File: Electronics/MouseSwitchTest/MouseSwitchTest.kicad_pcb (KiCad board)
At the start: 2 copper layers, 20.3 x 19.1 mm, 4 parts

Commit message: updated the middle click pcb
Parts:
- moved VDD1 14.1 mm to (13.5, 6.76)
- moved GPIO1 9.00 mm to (10.9, 6.76)
- moved S1 5.10 mm to (7.05, 0.00), turned to 180 degrees
- moved NC1 3.92 mm to (8.41, 6.76)
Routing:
- net Net-(NC1-Pin): track 7.81 -> 11.1 mm
- net Net-(GPIO1-Pin): track 6.76 -> 8.37 mm
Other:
- board size 20.3 x 19.1 mm -> 23.5 x 18.9 mm
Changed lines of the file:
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@@
 	(footprint "BardBarian_Footprints:Header"
 		(layer "F.Cu")
-		(at 4.49 6.7554)
+		(at 8.41 6.7554)
 		(property "Reference" "NC1"
-			(at 1.81 2.0446 0)
+			(at -1.91 2.0446 0)
 			(unlocked yes)
 			(layer "F.SilkS")
@@
 			)
 		)
-		(sheetname "Root")
-		(sheetfile "MouseSwitchTest.kicad_sch")
 		(attr through_hole)
 		(fp_rect
@@
 			)
 			(fill none)
+			(layer "F.SilkS")
+		)
+		(fp_rect
+			(start -1.27 -1.27)
+			(end 1.27 1.27)
+			(stroke
+				(width 0.1)
+				(type default)
+			)
+			(fill none)
 			(layer "Dwgs.User")
 		)
 		(fp_text user "${REFERENCE}"
-			(at 1.81 2.0446 0)
+			(at -1.91 2.0446 0)
 			(unlocked yes)
 			(layer "F.Fab")
@@
 	(footprint "BardBarian_Footprints:Header"
 		(layer "F.Cu")
-		(at -0.59 6.7554)
+		(at 13.49 6.7554)
 		(property "Reference" "VDD1"
-			(at -1.91 2.0446 0)
+			(at 2.51 2.0446 0)
 			(unlocked yes)
 			(layer "F.SilkS")
@@
 			)
 		)
-		(sheetname "Root")
-		(sheetfile "MouseSwitchTest.kicad_sch")
 		(attr through_hole)
 		(fp_rect
@@
 			)
 			(fill none)
+			(layer "F.SilkS")
+		)
+		(fp_rect
+			(start -1.27 -1.27)
+			(end 1.27 1.27)
+			(stroke
+				(width 0.1)
+				(type default)
+			)
+			(fill none)
 			(layer "Dwgs.User")
 		)
 		(fp_text user "${REFERENCE}"
-			(at -1.91 2.0446 0)
+			(at 2.51 2.0446 0)
 			(unlocked yes)
 			(layer "F.Fab")
@@
 	(footprint "BardBarian_Footprints:Header"
 		(layer "F.Cu")
-		(at 1.95 6.7554)
+		(at 10.95 6.7554)
 		(property "Reference" "GPIO1"
 			(at 0.05 2.0446 0)
@@
 			)
 		)
-		(sheetname "Root")
-		(sheetfile "MouseSwitchTest.kicad_sch")
 		(attr through_hole)
+		(fp_rect
+			(start -1.27 -1.27)
+			(end 1.27 1.27)
+			(stroke
+				(width 0.1)
+				(type default)
+			)
+			(fill none)
+			(layer "F.SilkS")
+		)
 		(fp_rect
 			(start -1.27 -1.27)
@@
 	(footprint "BardBarian_Footprints:Kailh GM 4.0 Red CMI126601D01"
 		(layer "F.Cu")
-		(at 1.95 0)
+		(at 7.05 0 180)
 		(property "Reference" "S1"
-			(at 0.05 3.9 0)
+			(at 0.05 3.9 180)
 			(unlocked yes)
 			(layer "F.SilkS")
@@
 		)
 		(property "Value" "~"
-			(at 0 1 0)
+			(at 0 1 180)
 			(unlocked yes)
 			(layer "F.Fab")
@@
 		)
 		(property "Footprint" "BardBarian_Footprints:Kailh GM 4.0 Red CMI126601D01"
-			(at 0 0 0)
+			(at 0 0 180)
 			(unlocked yes)
 			(layer "F.Fab")
@@
 		)
 		(property "Datasheet" ""
-			(at 0 0 0)
+			(at 0 0 180)
 			(unlocked yes)
 			(layer "F.Fab")
@@
 		)
 		(property "Description" ""
-			(at 0 0 0)
-			(unlocked yes)
-			(layer "F.Fab")
-			(hide yes)
-			(effects
-				(font
-					(size 1 1)
-					(thickness 0.15)
-				)
-			)
-		)
-		(sheetname "Root")
-		(sheetfile "MouseSwitchTest.kicad_sch")
+			(at 0 0 180)
+			(unlocked yes)
+			(layer "F.Fab")
+			(hide yes)
+			(effects
+				(font
+					(size 1 1)
+					(thickness 0.15)
+				)
+			)
+		)
 		(attr through_hole)
+		(fp_rect
+			(start -2.55 -1.45)
+			(end -1.35 1.45)
+			(stroke
+				(width 0.1)
+				(type default)
+			)
+			(fill none)
+			(layer "F.SilkS")
+		)
 		(fp_rect
 			(start -6.4 -2.9)
@@
 			)
 			(fill none)
-			(layer "F.SilkS")
+			(layer "Dwgs.User")
 		)
 		(fp_rect
@@
 			(layer "Dwgs.User")
 		)
-		(fp_rect
-			(start -2.55 -1.45)
-			(end -1.35 1.45)
-			(stroke
-				(width 0.1)
-				(type default)
-			)
-			(fill none)
-			(layer "Dwgs.User")
-		)
 		(fp_text user "${REFERENCE}"
-			(at 0.05 3.9 0)
+			(at 0.05 3.9 180)
 			(unlocked yes)
 			(layer "F.Fab")
@@
 		)
 		(pad "1" thru_hole circle
-			(at -5.08 0)
+			(at -5.08 0 180)
 			(size 1.8 1.8)
 			(drill 1.1)
@@
 		)
 		(pad "2" thru_hole circle
-			(at 0 0)
+			(at 0 0 180)
 			(size 1.8 1.8)
 			(drill 1.1)
@@
 		)
 		(pad "3" thru_hole circle
-			(at 5.08 0)
+			(at 5.08 0 180)
 			(size 1.8 1.8)
 			(drill 1.1)
@@
 	)
 	(gr_circle
-		(center 10 6)
-		(end 11.6 6)
+		(center 20.05 -6)
+		(end 21.32 -6)
 		(stroke
 			(width 0.05)
@@
 		)
 		(fill none)
-		(layer "Edge.Cuts")
+		(layer "F.SilkS")
 	)
 	(gr_circle
-		(center 10 -6)
-		(end 11.6 -6)
+		(center 20.05 6)
+		(end 21.32 6)
 		(stroke
 			(width 0.05)
@@
 		)
 		(fill none)
+		(layer "F.SilkS")
+	)
+	(gr_circle
+		(center 20.05 6)
+		(end 20.9 6)
+		(stroke
+			(width 0.05)
+			(type default)
+		)
+		(fill none)
 		(layer "Edge.Cuts")
 	)
+	(gr_circle
+		(center 20.05 -6)
+		(end 20.9 -6)
+		(stroke
+			(width 0.05)
+			(type default)
+		)
+		(fill none)
+		(layer "Edge.Cuts")
+	)
 	(gr_rect
-		(start -7.78 -9.525)
-		(end 12.525 9.525)
+		(start -1.33 9.475)
+		(end 22.12 -9.425)
 		(stroke
 			(width 0.2)
@@
 	)
 	(segment
-		(start 1.95 0)
-		(end 1.95 6.7554)
+		(start 7.05 0)
+		(end 7.05 2.8554)
 		(width 0.2)
 		(layer "F.Cu")
@@
 	)
 	(segment
-		(start -3.13 4.2154)
-		(end -0.59 6.7554)
+		(start 7.05 2.8554)
+		(end 10.95 6.7554)
+		(width 0.2)
+		(layer "F.Cu")
+		(net 1)
+	)
+	(segment
+		(start 13.49 1.36)
+		(end 13.49 6.7554)
 		(width 0.2)
 		(layer "F.Cu")
@@
 	)
 	(segment
-		(start -3.13 0)
-		(end -3.13 4.2154)
+		(start 12.13 0)
+		(end 13.49 1.36)
 		(width 0.2)
 		(layer "F.Cu")
@@
 	)
 	(segment
-		(start 7.03 0)
-		(end 7.03 4.2154)
+		(start 1.97 3.17)
+		(end 5.5554 6.7554)
 		(width 0.2)
 		(layer "F.Cu")
@@
 	)
 	(segment
-		(start 7.03 4.2154)
-		(end 4.49 6.7554)
-		(width 0.2)
-		(layer "F.Cu")
+		(start 5.5554 6.7554)
+		(end 8.41 6.7554)
+		(width 0.2)
+		(layer "F.Cu")
+		(net 3)
+	)
+	(segment
+		(start 1.97 0)
+		(end 1.97 3.17)
+		(width 0.2)
+		(layer "F.Cu")

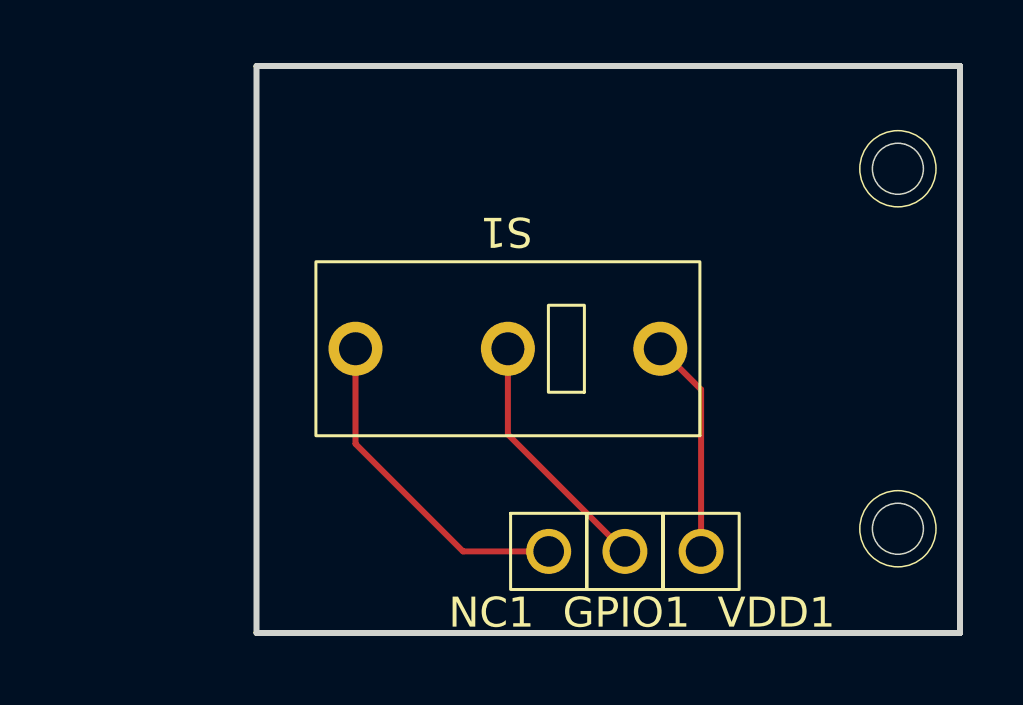
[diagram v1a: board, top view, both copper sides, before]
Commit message: rotated the middle click mouse switch to avoid collisions with the assistive springs
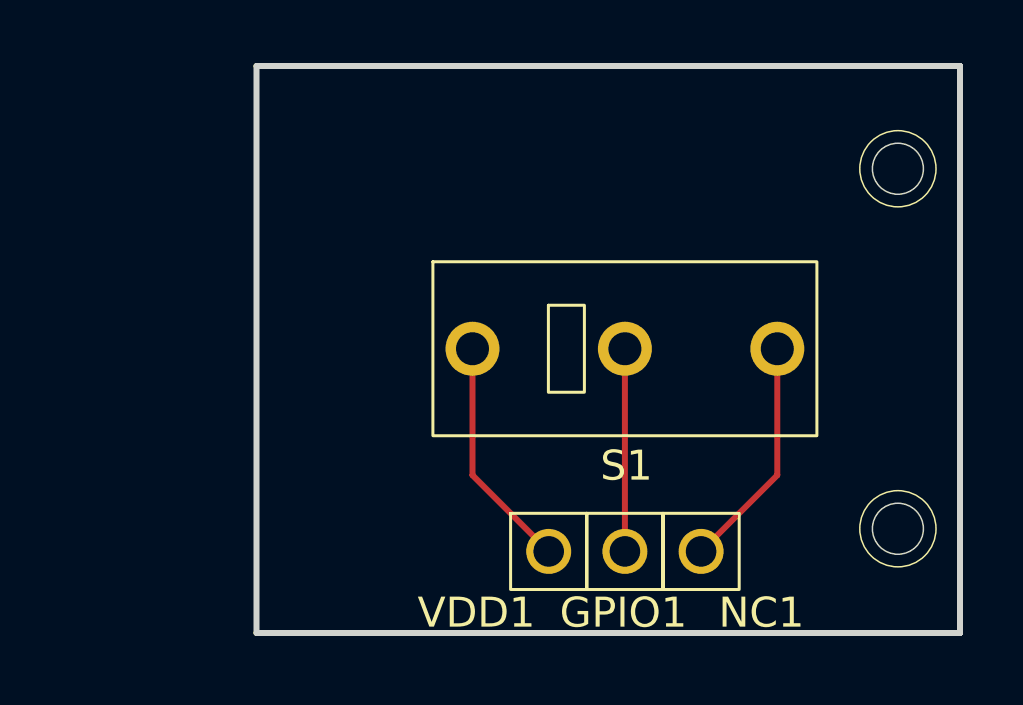
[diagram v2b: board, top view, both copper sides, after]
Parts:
- moved NC1 5.08 mm to (13.5, 6.76)
- moved VDD1 5.08 mm to (8.41, 6.76)
- moved S1 3.90 mm to (10.9, 0.00), turned to 0 degrees
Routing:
- net Net-(NC1-Pin): track 11.1 -> 7.81 mm
- net Net-(GPIO1-Pin): track 8.37 -> 6.76 mm
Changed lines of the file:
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@@
 	(footprint "BardBarian_Footprints:Header"
 		(layer "F.Cu")
-		(at 8.41 6.7554)
+		(at 13.49 6.7554)
 		(property "Reference" "NC1"
-			(at -1.91 2.0446 0)
+			(at 2.01 2.0446 0)
 			(unlocked yes)
 			(layer "F.SilkS")
@@
 		)
 		(fp_text user "${REFERENCE}"
-			(at -1.91 2.0446 0)
+			(at 2.01 2.0446 0)
 			(unlocked yes)
 			(layer "F.Fab")
@@
 	(footprint "BardBarian_Footprints:Header"
 		(layer "F.Cu")
-		(at 13.49 6.7554)
+		(at 8.41 6.7554)
 		(property "Reference" "VDD1"
-			(at 2.51 2.0446 0)
+			(at -2.41 2.0446 0)
 			(unlocked yes)
 			(layer "F.SilkS")
@@
 		)
 		(fp_text user "${REFERENCE}"
-			(at 2.51 2.0446 0)
+			(at -2.41 2.0446 0)
 			(unlocked yes)
 			(layer "F.Fab")
@@
 		(at 10.95 6.7554)
 		(property "Reference" "GPIO1"
-			(at 0.05 2.0446 0)
+			(at -0.05 2.0446 0)
 			(unlocked yes)
 			(layer "F.SilkS")
@@
 		)
 		(fp_text user "${REFERENCE}"
-			(at 0.05 2.0446 0)
+			(at -0.05 2.0446 0)
 			(unlocked yes)
 			(layer "F.Fab")
@@
 	(footprint "BardBarian_Footprints:Kailh GM 4.0 Red CMI126601D01"
 		(layer "F.Cu")
-		(at 7.05 0 180)
+		(at 10.95 0)
 		(property "Reference" "S1"
-			(at 0.05 3.9 180)
+			(at 0.05 3.9 0)
 			(unlocked yes)
 			(layer "F.SilkS")
@@
 		)
 		(property "Value" "~"
-			(at 0 1 180)
+			(at 0 1 0)
 			(unlocked yes)
 			(layer "F.Fab")
@@
 		)
 		(property "Footprint" "BardBarian_Footprints:Kailh GM 4.0 Red CMI126601D01"
-			(at 0 0 180)
+			(at 0 0 0)
 			(unlocked yes)
 			(layer "F.Fab")
@@
 		)
 		(property "Datasheet" ""
-			(at 0 0 180)
+			(at 0 0 0)
 			(unlocked yes)
 			(layer "F.Fab")
@@
 		)
 		(property "Description" ""
-			(at 0 0 180)
+			(at 0 0 0)
 			(unlocked yes)
 			(layer "F.Fab")
@@
 		)
 		(attr through_hole)
+		(fp_rect
+			(start -6.4 -2.9)
+			(end 6.4 2.9)
+			(stroke
+				(width 0.1)
+				(type default)
+			)
+			(fill none)
+			(layer "F.SilkS")
+		)
 		(fp_rect
 			(start -2.55 -1.45)
@@
 			)
 			(fill none)
-			(layer "F.SilkS")
+			(layer "Dwgs.User")
 		)
 		(fp_rect
@@
 			(layer "Dwgs.User")
 		)
-		(fp_rect
-			(start -6.4 -2.9)
-			(end 6.4 2.9)
-			(stroke
-				(width 0.1)
-				(type default)
-			)
-			(fill none)
-			(layer "Dwgs.User")
-		)
 		(fp_text user "${REFERENCE}"
-			(at 0.05 3.9 180)
+			(at 0.05 3.9 0)
 			(unlocked yes)
 			(layer "F.Fab")
@@
 		)
 		(pad "1" thru_hole circle
-			(at -5.08 0 180)
+			(at -5.08 0)
 			(size 1.8 1.8)
 			(drill 1.1)
@@
 		)
 		(pad "2" thru_hole circle
-			(at 0 0 180)
+			(at 0 0)
 			(size 1.8 1.8)
 			(drill 1.1)
@@
 		)
 		(pad "3" thru_hole circle
-			(at 5.08 0 180)
+			(at 5.08 0)
 			(size 1.8 1.8)
 			(drill 1.1)
@@
 	)
 	(gr_rect
-		(start -1.33 9.475)
-		(end 22.12 -9.425)
+		(start -1.33 -9.425)
+		(end 22.12 9.475)
 		(stroke
 			(width 0.2)
@@
 	)
 	(segment
-		(start 7.05 0)
-		(end 7.05 2.8554)
-		(width 0.2)
-		(layer "F.Cu")
-		(net 1)
-	)
-	(segment
-		(start 7.05 2.8554)
+		(start 10.95 0)
 		(end 10.95 6.7554)
 		(width 0.2)
@@
 	)
 	(segment
-		(start 13.49 1.36)
+		(start 5.87 4.2154)
+		(end 8.41 6.7554)
+		(width 0.2)
+		(layer "F.Cu")
+		(net 2)
+	)
+	(segment
+		(start 5.87 0)
+		(end 5.87 4.2154)
+		(width 0.2)
+		(layer "F.Cu")
+		(net 2)
+	)
+	(segment
+		(start 16.03 0)
+		(end 16.03 4.2154)
+		(width 0.2)
+		(layer "F.Cu")
+		(net 3)
+	)
+	(segment
+		(start 16.03 4.2154)
 		(end 13.49 6.7554)
 		(width 0.2)
 		(layer "F.Cu")
-		(net 2)
-	)
-	(segment
-		(start 12.13 0)
-		(end 13.49 1.36)
-		(width 0.2)
-		(layer "F.Cu")
-		(net 2)
-	)
-	(segment
-		(start 1.97 3.17)
-		(end 5.5554 6.7554)
-		(width 0.2)
-		(layer "F.Cu")
-		(net 3)
-	)
-	(segment
-		(start 5.5554 6.7554)
-		(end 8.41 6.7554)
-		(width 0.2)
-		(layer "F.Cu")
-		(net 3)
-	)
-	(segment
-		(start 1.97 0)
-		(end 1.97 3.17)
-		(width 0.2)
-		(layer "F.Cu")
